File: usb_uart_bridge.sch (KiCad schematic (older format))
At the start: 7 parts, among them U2 CP2102N-A01-GQFN28

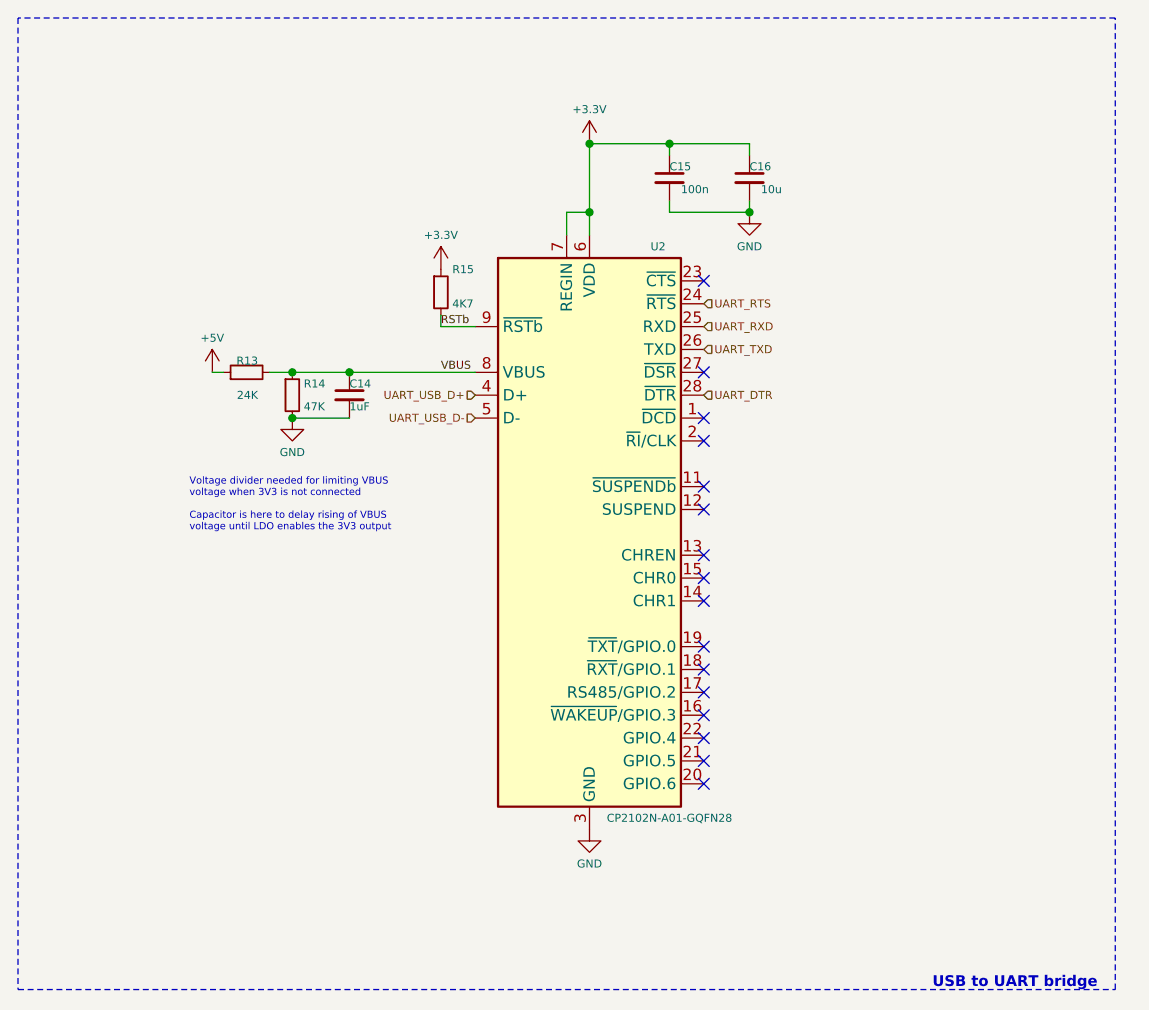
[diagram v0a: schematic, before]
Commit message: Replace CP2102 with CH340X
Also add BJTs to ESP32C3 strapping pins
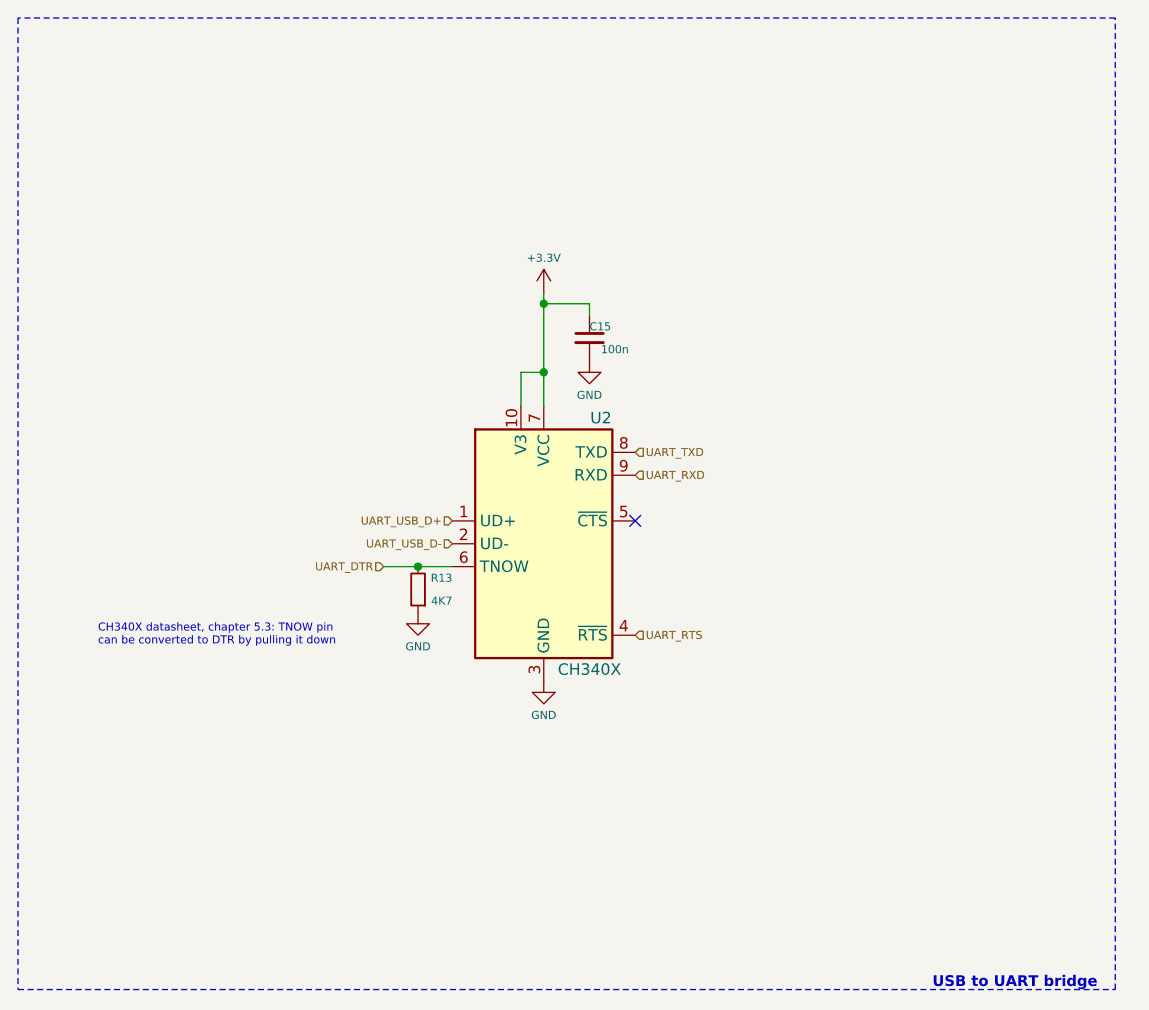
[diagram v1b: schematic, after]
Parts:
- removed C14: 1uF, Capacitor_SMD:C_0402_1005Metric, symbol Device:C_Small
- removed C16: 10u, Capacitor_SMD:C_0603_1608Metric, symbol Device:C_Small
- removed R14: 47K, Resistor_SMD:R_0402_1005Metric, symbol Device:R_Small
- removed R15: 4K7, Resistor_SMD:R_0402_1005Metric, symbol Device:R_Small
- removed U2: CP2102N-A01-GQFN28, Package_DFN_QFN:QFN-28-1EP_5x5mm_P0.5mm_EP3.35x3.35mm, symbol Interface_USB:CP2102N-A01-GQFN28
- added U2: CH340X, Package_SO:MSOP-10_3x3mm_P0.5mm, symbol Interface_USB:CH340E
- R13: value 24K -> 4K7; LCSC C25769 -> C21190
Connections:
- net +5V is gone; now on net GND: R13.1
- net VBUS is gone; now on net UART_DTR: R13.2
- net +3V3: now also U2.10 (V3), U2.7 (VCC)
- net GND: now also U2.3 (GND)
- net UART_DTR: now also U2.6 (TNOW)
- net UART_RTS: now also U2.4 (~RTS)
- net UART_RXD: now also U2.9 (RXD)
- net UART_TXD: now also U2.8 (TXD)
- net UART_USB_D+: now also U2.1 (UD+)
- net UART_USB_D-: now also U2.2 (UD-)
- no-connect marks 16 -> 1
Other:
- note added: "CH340X datasheet, chapter 5.3: TNOW pin\ncan be converted to DTR by pulling it down"
- note removed: "Voltage divider needed for limiting VBUS\nvoltage when 3V3 is not connected\n\nCapacitor is here to delay rising of VBUS\nvoltage until LDO enables the 3V3 output"

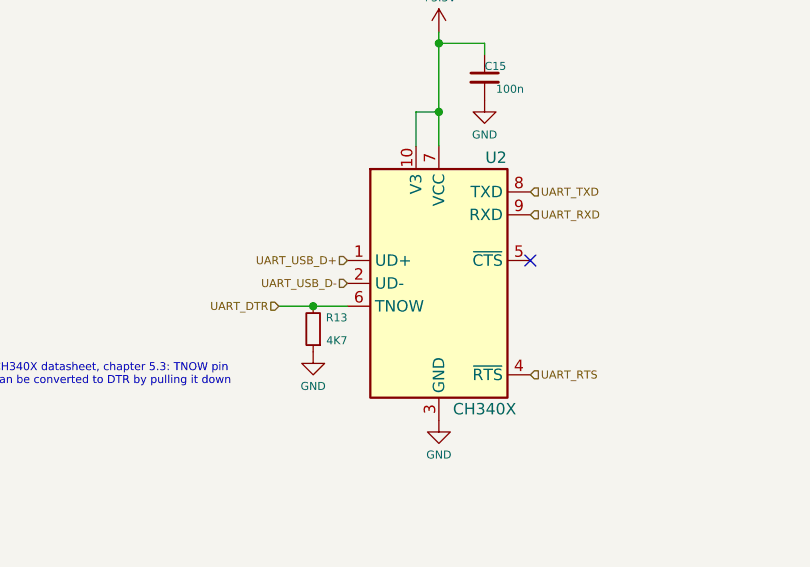
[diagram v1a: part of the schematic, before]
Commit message: Use ESP32-C3-WROOM-02 module
Signed-off-by: Tomislav Milkovic <tomislav.milkovic95@gmail.com>
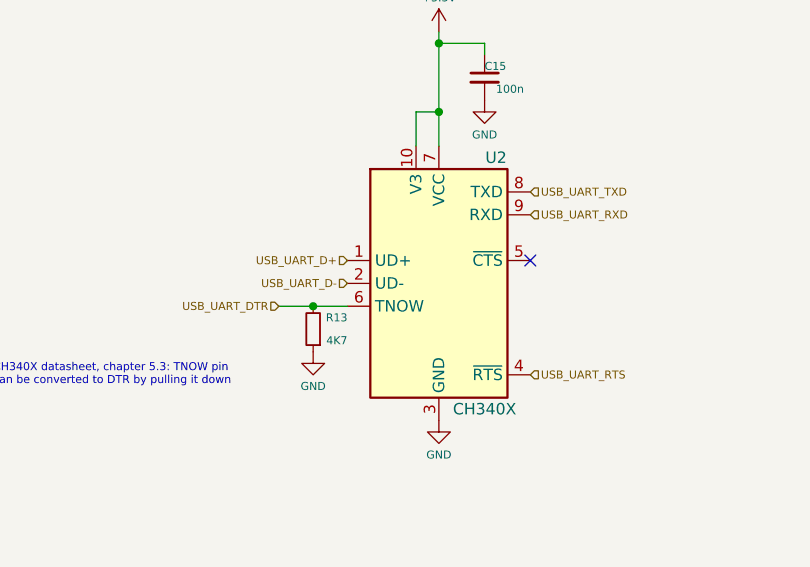
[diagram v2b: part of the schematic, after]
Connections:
- net UART_DTR renamed USB_UART_DTR
- net UART_RTS renamed USB_UART_RTS
- net UART_RXD renamed USB_UART_RXD
- net UART_TXD renamed USB_UART_TXD
- net UART_USB_D+ renamed USB_UART_D+
- net UART_USB_D- renamed USB_UART_D-
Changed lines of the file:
@@
 $Descr A4 11693 8268
 encoding utf-8
-Sheet 3 5
+Sheet 5 5
 Title "USB-UART bridge"
 Date "2022-11-20"
@@
 $EndComp
 Text HLabel 2400 2700 0    35   Input ~ 0
-UART_USB_D+
+USB_UART_D+
 Text HLabel 2400 2800 0    35   Input ~ 0
-UART_USB_D-
+USB_UART_D-
 Text HLabel 2100 2900 0    35   Input ~ 0
-UART_DTR
+USB_UART_DTR
 Text HLabel 3200 3200 2    35   Input ~ 0
-UART_RTS
+USB_UART_RTS
 NoConn ~ 3200 2700
 Text HLabel 3200 2500 2    35   Input ~ 0
-UART_RXD
+USB_UART_RXD
 Text HLabel 3200 2400 2    35   Input ~ 0
-UART_TXD
+USB_UART_TXD
 $Comp
 L power:GND #PWR?

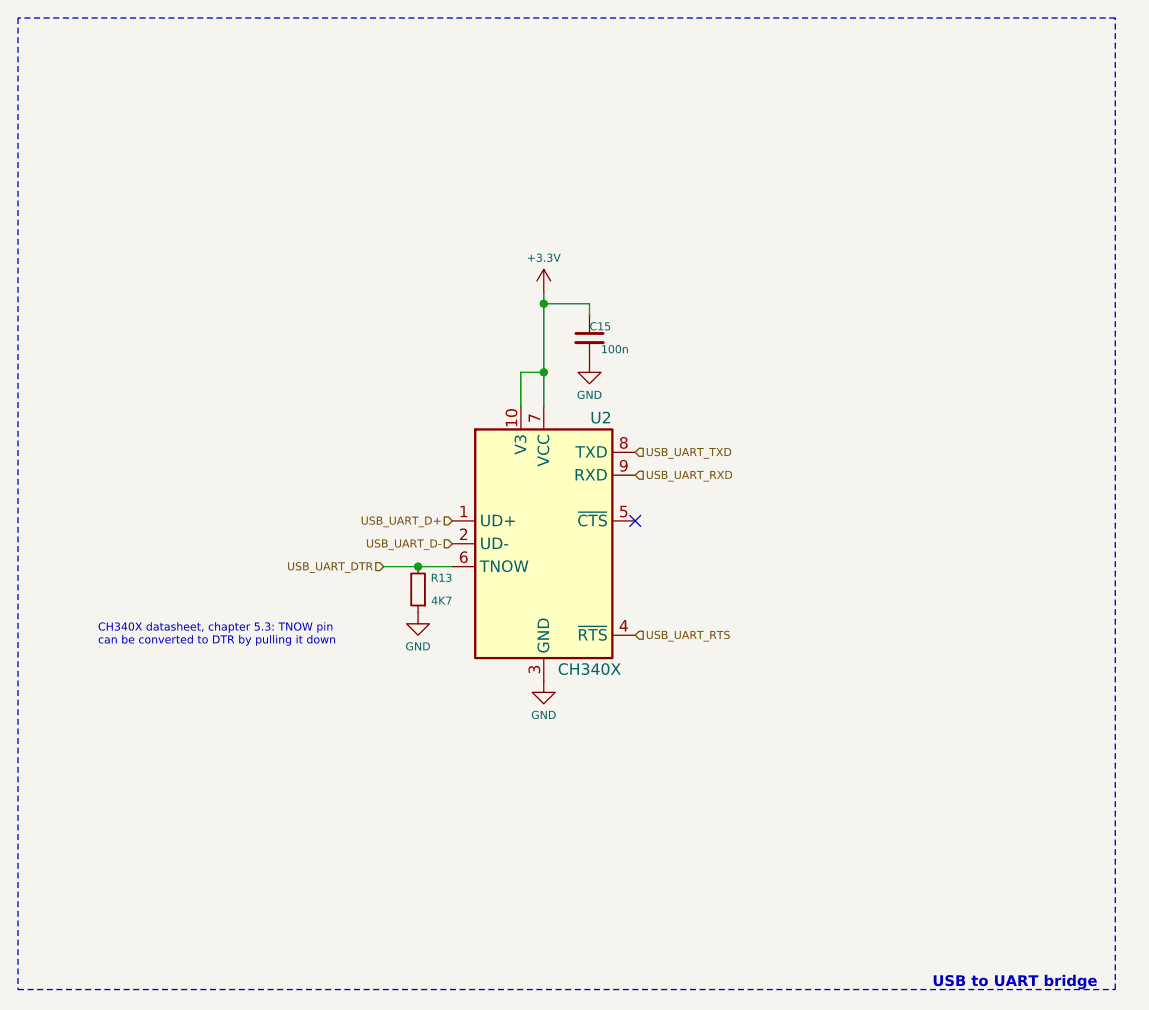
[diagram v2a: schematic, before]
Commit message: Change USB UART adapter to CP2102
Signed-off-by: Tomislav Milkovic <tomislav.milkovic95@gmail.com>
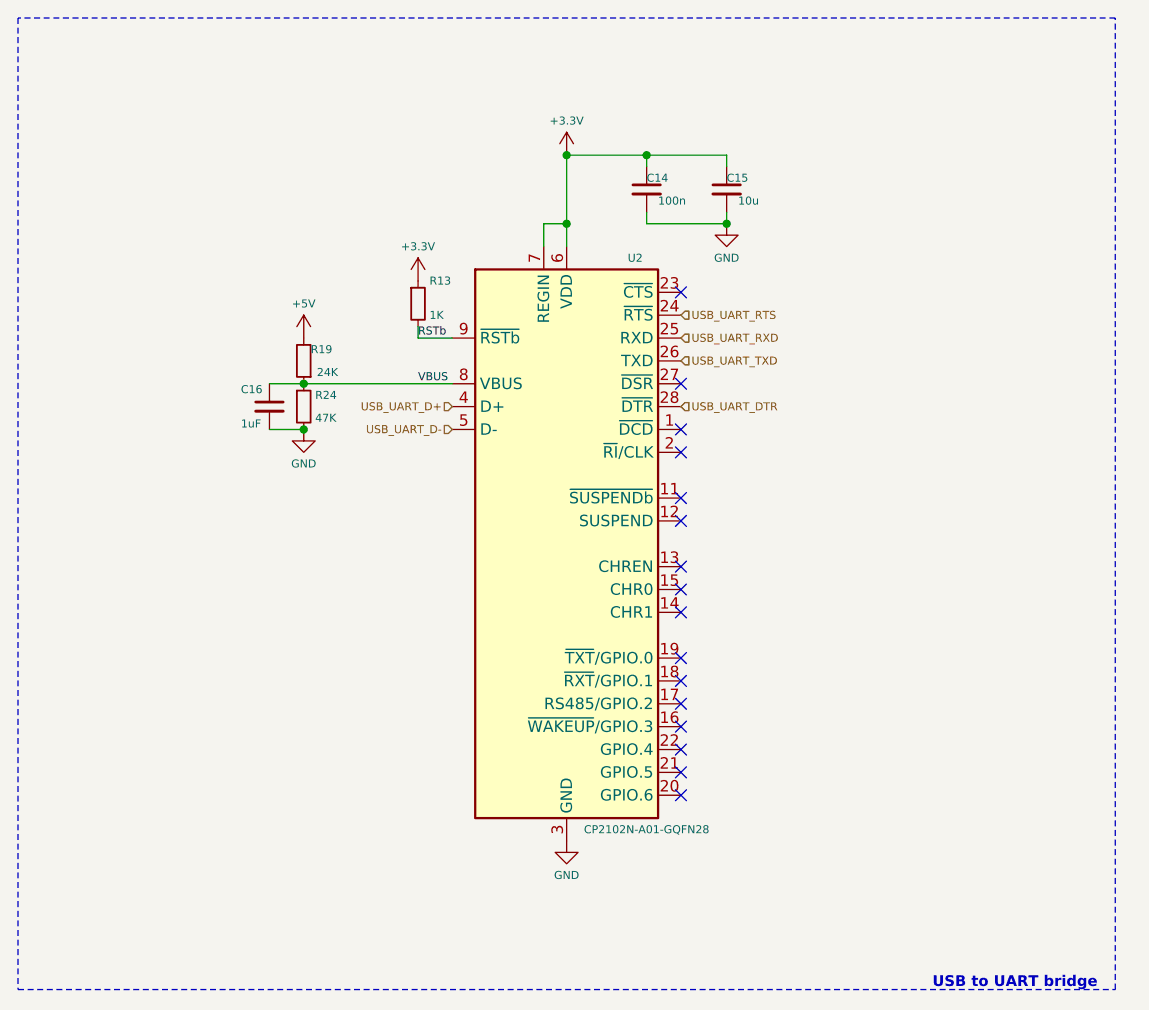
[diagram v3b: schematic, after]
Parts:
- removed U2: CH340X, Package_SO:MSOP-10_3x3mm_P0.5mm, symbol Interface_USB:CH340E
- added C14: 100n, Capacitor_SMD:C_0402_1005Metric, symbol Device:C_Small
- added C16: 1uF, Capacitor_SMD:C_0402_1005Metric, symbol Device:C_Small
- added R19: 24K, Resistor_SMD:R_0402_1005Metric, symbol Device:R_Small
- added R24: 47K, Resistor_SMD:R_0402_1005Metric, symbol Device:R_Small
- added U2: CP2102N-A01-GQFN28, Package_DFN_QFN:QFN-28-1EP_5x5mm_P0.5mm_EP3.35x3.35mm, symbol Interface_USB:CP2102N-A01-GQFN28
- C15: value 100n -> 10u; footprint Capacitor_SMD:C_0402_1005Metric -> Capacitor_SMD:C_0805_2012Metric; LCSC C307331 -> C440198
- R13: value 4K7 -> 1K; LCSC C21190 -> C25900
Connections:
- net +3V3: now also R13.1, C14.1, U2.6 (VDD), U2.7 (REGIN)
- net GND: now also C14.2, C16.2, R24.2, U2.29 (GND), U2.3 (GND); no longer R13.1
- net USB_UART_D+: now also U2.4 (D+)
- net USB_UART_D-: now also U2.5 (D-)
- net USB_UART_DTR: now also U2.28 (~DTR); no longer R13.2
- net USB_UART_RTS: now also U2.24 (~RTS)
- net USB_UART_RXD: now also U2.25 (RXD)
- net USB_UART_TXD: now also U2.26 (TXD)
- new net +5V: R19.2
- new net RSTb: R13.2, U2.9 (~RSTb)
- new net VBUS: C16.1, R19.1, R24.1, U2.8 (VBUS)
- no-connect marks 1 -> 16
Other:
- note removed: "CH340X datasheet, chapter 5.3: TNOW pin\ncan be converted to DTR by pulling it down"

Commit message: Add LCSC part numbers for all components
Signed-off-by: Tomislav Milkovic <tomislav.milkovic95@gmail.com>
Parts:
- C15: footprint Capacitor_SMD:C_0805_2012Metric -> Capacitor_SMD:C_0603_1608Metric; LCSC C440198 -> C19702
- R13: LCSC C25900 -> C11702
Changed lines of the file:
@@
 Sheet 5 5
 Title "USB-UART bridge"
-Date "2022-11-20"
+Date "2025-02-16"
 Rev "1.0"
 Comp "Copyright: Tomislav Milkovic"
@@
 F 1 "1K" H 2300 1700 35  0000 L CNN
 F 2 "Resistor_SMD:R_0402_1005Metric" H 2250 1750 50  0001 C CNN
-F 3 "https://datasheet.lcsc.com/lcsc/2206010045_UNI-ROYAL-Uniroyal-Elec-0402WGF4701TCE_C25900.pdf" H 2250 1750 50  0001 C CNN
-F 4 "C25900" H 2250 1750 50  0001 C CNN "LCSC"
+F 3 "https://www.lcsc.com/datasheet/lcsc_datasheet_2206010216_UNI-ROYAL-Uniroyal-Elec-0402WGF1001TCE_C11702.pdf" H 2250 1750 50  0001 C CNN
+F 4 "C11702" H 2250 1750 50  0001 C CNN "LCSC"
 	1    2250 1750
 	1    0    0    -1
@@
 U 1 1 67B22DEB
 P 1750 2000
-F 0 "R19" H 1625 1950 35  0000 L CNN
+F 0 "R19" H 1600 1950 35  0000 L CNN
 F 1 "24K" H 1600 2050 35  0000 L CNN
 F 2 "Resistor_SMD:R_0402_1005Metric" H 1750 2000 50  0001 C CNN
@@
 F 0 "C15" H 3600 1300 35  0000 L CNN
 F 1 "10u" H 3650 1200 35  0000 L CNN
-F 2 "Capacitor_SMD:C_0805_2012Metric" H 3600 1250 50  0001 C CNN
+F 2 "Capacitor_SMD:C_0603_1608Metric" H 3600 1250 50  0001 C CNN
 F 3 "https://datasheet.lcsc.com/lcsc/2004251506_Murata-Electronics-GRM21BR61H106KE43L_C440198.pdf" H 3600 1250 50  0001 C CNN
-F 4 "C440198" H 3600 1250 50  0001 C CNN "LCSC"
+F 4 "C19702" H 3600 1250 50  0001 C CNN "LCSC"
 	1    3600 1250
 	1    0    0    -1

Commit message: PCB: Rough component placement done
Signed-off-by: Tomislav Milkovic <tomislav.milkovic95@gmail.com>
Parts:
- renumbered C14 to C15, C15 to C16, C16 to C17, R13 to R16, R19 to R17, R24 to R18, U2 to U4
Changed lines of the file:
@@
 	500  500  500  4750
 $Comp
-L Interface_USB:CP2102N-A01-GQFN28 U2
+L Interface_USB:CP2102N-A01-GQFN28 U4
 U 1 1 67B22DA7
 P 2900 2800
-F 0 "U2" H 3200 4050 35  0000 C CNN
+F 0 "U4" H 3200 4050 35  0000 C CNN
 F 1 "CP2102N-A01-GQFN28" H 3250 1550 35  0000 C CNN
 F 2 "Package_DFN_QFN:QFN-28-1EP_5x5mm_P0.5mm_EP3.35x3.35mm" H 3350 1600 50  0001 L CNN
@@
 $EndComp
 $Comp
-L Device:R_Small R13
+L Device:R_Small R16
 U 1 1 67B22DC6
 P 2250 1750
-F 0 "R13" H 2300 1850 35  0000 L CNN
+F 0 "R16" H 2300 1850 35  0000 L CNN
 F 1 "1K" H 2300 1700 35  0000 L CNN
 F 2 "Resistor_SMD:R_0402_1005Metric" H 2250 1750 50  0001 C CNN
@@
 	2900 1400 2900 1500
 $Comp
-L Device:C_Small C14
+L Device:C_Small C15
 U 1 1 67B22DE4
 P 3250 1250
-F 0 "C14" H 3250 1300 35  0000 L CNN
+F 0 "C15" H 3250 1300 35  0000 L CNN
 F 1 "100n" H 3300 1200 35  0000 L CNN
 F 2 "Capacitor_SMD:C_0402_1005Metric" H 3250 1250 50  0001 C CNN
@@
 $EndComp
 $Comp
-L Device:R_Small R19
+L Device:R_Small R17
 U 1 1 67B22DEB
 P 1750 2000
-F 0 "R19" H 1600 1950 35  0000 L CNN
+F 0 "R17" H 1600 1950 35  0000 L CNN
 F 1 "24K" H 1600 2050 35  0000 L CNN
 F 2 "Resistor_SMD:R_0402_1005Metric" H 1750 2000 50  0001 C CNN
@@
 $EndComp
 $Comp
-L Device:R_Small R24
+L Device:R_Small R18
 U 1 1 67B22DF8
 P 1750 2200
-F 0 "R24" H 1800 2250 35  0000 L CNN
+F 0 "R18" H 1800 2250 35  0000 L CNN
 F 1 "47K" H 1800 2150 35  0000 L CNN
 F 2 "Resistor_SMD:R_0402_1005Metric" H 1750 2200 50  0001 C CNN
@@
 $EndComp
 $Comp
-L Device:C_Small C16
+L Device:C_Small C17
 U 1 1 67B22E00
 P 1600 2200
-F 0 "C16" H 1475 2275 35  0000 L CNN
+F 0 "C17" H 1475 2275 35  0000 L CNN
 F 1 "1uF" H 1475 2125 35  0000 L CNN
 F 2 "Capacitor_SMD:C_0402_1005Metric" H 1600 2200 50  0001 C CNN
@@
 $EndComp
 $Comp
-L Device:C_Small C15
+L Device:C_Small C16
 U 1 1 67B22E12
 P 3600 1250
-F 0 "C15" H 3600 1300 35  0000 L CNN
+F 0 "C16" H 3600 1300 35  0000 L CNN
 F 1 "10u" H 3650 1200 35  0000 L CNN
 F 2 "Capacitor_SMD:C_0603_1608Metric" H 3600 1250 50  0001 C CNN

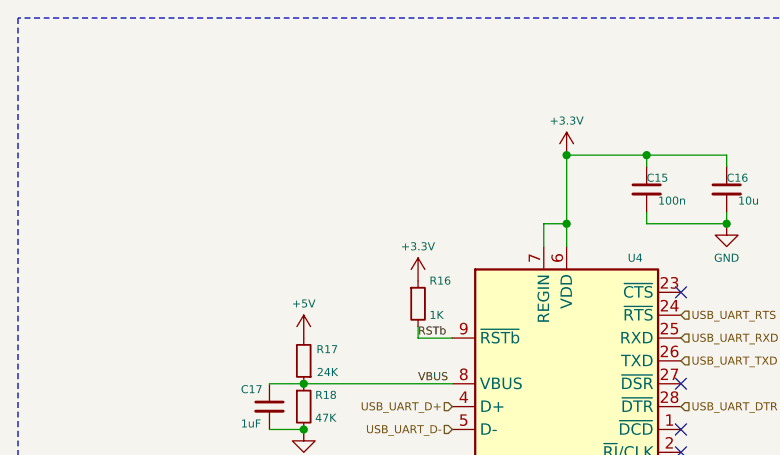
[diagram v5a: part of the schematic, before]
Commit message: Add fiducials, finish routing
Signed-off-by: Tomislav Milkovic <tomislav.milkovic95@gmail.com>
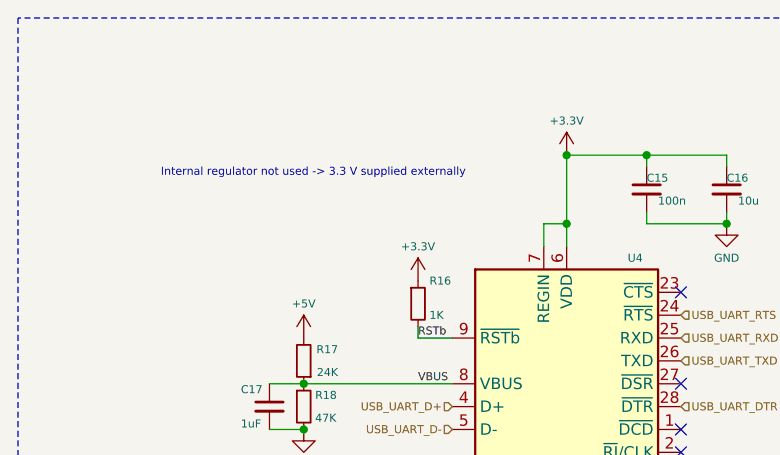
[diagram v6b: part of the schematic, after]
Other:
- note added: "Internal regulator not used -> 3.3 V supplied externally"
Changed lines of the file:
@@
 Wire Wire Line
 	1600 2300 1750 2300
+Text Notes 1125 1200 0    35   ~ 0
+Internal regulator not used -> 3.3 V supplied externally
 $EndSCHEMATC
